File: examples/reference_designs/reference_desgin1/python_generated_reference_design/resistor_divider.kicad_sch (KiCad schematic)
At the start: 3 parts

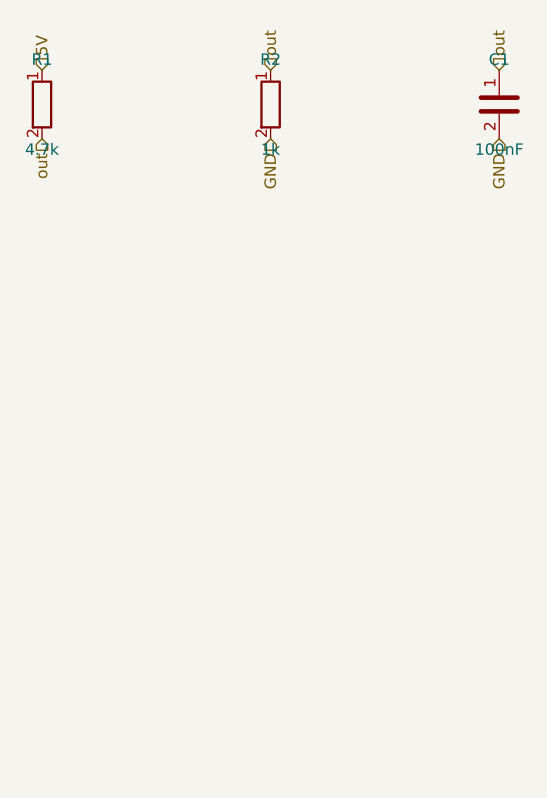
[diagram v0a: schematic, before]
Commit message: Fix component synchronization issue in reference design
Fixed issue where extra resistor components were being added back to KiCad
schematic after manual deletion. The problem was in the Python circuit
definition having both resistors with the same reference prefix "R",
causing synchronization mismatch.

Changes:
- Modified python_generated_reference_design.py to define only desired components
- Changed second resistor to explicit reference "R2" instead of prefix "R"
- Removed first resistor (r1) and its connections from circuit definition
- Updated project files to reflect synchronized state

🤖 Generated with [Claude Code](https://claude.ai/code)

Co-Authored-By: Claude <noreply@anthropic.com>
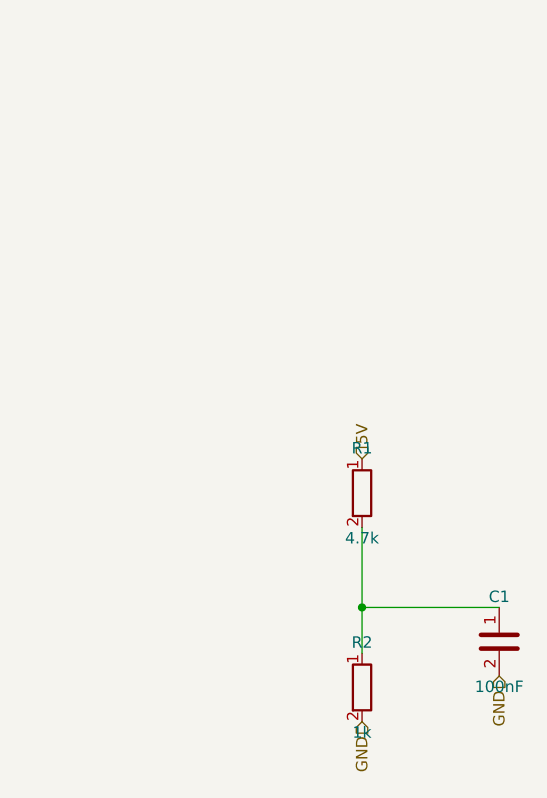
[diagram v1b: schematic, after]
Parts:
- C1, R1, R2: now left out of the parts list
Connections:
- net out: no longer names the net of C1.1, R1.2, R2.1
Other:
- company: (none) -> Circuit-Synth
- title: (none) -> resistor_divider
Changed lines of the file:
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@@
 (kicad_sch
 	(version 20250114)
-	(generator "circuit_synth")
+	(generator "eeschema")
 	(generator_version 9.0)
 	(paper A4)
+	(title_block
+		(title resistor_divider)
+		(date 2025-07-26)
+		(company Circuit-Synth)
+	)
 	(symbol
 		(lib_id Device:R)
-		(at 25.4 25.4 0)
-		(in_bom yes)
-		(on_board yes)
+		(at 60.96 90.17 0)
+		(in_bom no)
+		(on_board no)
+		(dnp no)
+		(property
+			"Reference"
+			"R2"
+			(at 60.96 85.17 0)
+			(effects
+				(font
+					(size 1.27 1.27)
+				)
+			)
+		)
+		(property
+			"Value"
+			"1k"
+			(at 60.96 95.17 0)
+			(effects
+				(font
+					(size 1.27 1.27)
+				)
+			)
+		)
+		(property
+			"Footprint"
+			"Resistor_SMD:R_0603_1608Metric"
+			(at 60.96 100.17 0)
+			(effects
+				(font
+					(size 1.27 1.27)
+				)
+				(hide yes)
+			)
+		)
+		(instances)
+	)
+	(symbol
+		(lib_id Device:C)
+		(at 76.2 85.09 0)
+		(in_bom no)
+		(on_board no)
+		(dnp no)
+		(property
+			"Reference"
+			"C1"
+			(at 76.2 80.09 0)
+			(effects
+				(font
+					(size 1.27 1.27)
+				)
+			)
+		)
+		(property
+			"Value"
+			"100nF"
+			(at 76.2 90.09 0)
+			(effects
+				(font
+					(size 1.27 1.27)
+				)
+			)
+		)
+		(property
+			"Footprint"
+			"Capacitor_SMD:C_0603_1608Metric"
+			(at 76.2 95.09 0)
+			(effects
+				(font
+					(size 1.27 1.27)
+				)
+				(hide yes)
+			)
+		)
+		(instances)
+	)
+	(symbol
+		(lib_id Device:R)
+		(at 60.96 68.58 0)
+		(in_bom no)
+		(on_board no)
 		(dnp no)
 		(property
 			"Reference"
 			"R1"
-			(at 25.4 20.4 0)
+			(at 60.96 63.58 0)
 			(effects
 				(font
@@
 			"Value"
 			"4.7k"
-			(at 25.4 30.4 0)
+			(at 60.96 73.58 0)
 			(effects
 				(font
@@
 			"Footprint"
 			"Resistor_SMD:R_0603_1608Metric"
-			(at 25.4 35.4 0)
+			(at 60.96 78.58 0)
 			(effects
 				(font
@@
 			)
 		)
-		(instances
-			(project
-				"python_generated_reference_design"
-				(path
-					"/548f32ab-3b72-47b6-b7c9-f49e04bff365/2b5db3a5-2db6-41cd-8ca2-ff5d8aed297d"
-					(reference R1)
-					(unit 1)
-				)
-			)
+		(instances)
+	)
+	(wire
+		(pts
+			(xy 60.96 81.28)
+			(xy 60.96 72.39)
+		)
+		(stroke
+			(width 0)
+			(type default)
 		)
 	)
-	(symbol
-		(lib_id Device:R)
-		(at 50.8 25.4 0)
-		(in_bom yes)
-		(on_board yes)
-		(dnp no)
-		(property
-			"Reference"
-			"R2"
-			(at 50.8 20.4 0)
-			(effects
-				(font
-					(size 1.27 1.27)
-				)
-			)
+	(wire
+		(pts
+			(xy 76.2 81.28)
+			(xy 60.96 81.28)
 		)
-		(property
-			"Value"
-			"1k"
-			(at 50.8 30.4 0)
-			(effects
-				(font
-					(size 1.27 1.27)
-				)
-			)
-		)
-		(property
-			"Footprint"
-			"Resistor_SMD:R_0603_1608Metric"
-			(at 50.8 35.4 0)
-			(effects
-				(font
-					(size 1.27 1.27)
-				)
-				(hide yes)
-			)
-		)
-		(instances
-			(project
-				"python_generated_reference_design"
-				(path
-					"/548f32ab-3b72-47b6-b7c9-f49e04bff365/2b5db3a5-2db6-41cd-8ca2-ff5d8aed297d"
-					(reference R2)
-					(unit 1)
-				)
-			)
+		(stroke
+			(width 0)
+			(type default)
 		)
 	)
-	(symbol
-		(lib_id Device:C)
-		(at 76.2 25.4 0)
-		(in_bom yes)
-		(on_board yes)
-		(dnp no)
-		(property
-			"Reference"
-			"C1"
-			(at 76.2 20.4 0)
-			(effects
-				(font
-					(size 1.27 1.27)
-				)
-			)
+	(wire
+		(pts
+			(xy 60.96 81.28)
+			(xy 60.96 86.36)
 		)
-		(property
-			"Value"
-			"100nF"
-			(at 76.2 30.4 0)
-			(effects
-				(font
-					(size 1.27 1.27)
-				)
-			)
-		)
-		(property
-			"Footprint"
-			"Capacitor_SMD:C_0603_1608Metric"
-			(at 76.2 35.4 0)
-			(effects
-				(font
-					(size 1.27 1.27)
-				)
-				(hide yes)
-			)
-		)
-		(instances
-			(project
-				"python_generated_reference_design"
-				(path
-					"/548f32ab-3b72-47b6-b7c9-f49e04bff365/2b5db3a5-2db6-41cd-8ca2-ff5d8aed297d"
-					(reference C1)
-					(unit 1)
-				)
-			)
+		(stroke
+			(width 0)
+			(type default)
 		)
 	)
@@
 		5V
 		(shape input)
-		(at 25.4 21.59 90)
-		(effects
-			(font
-				(size 1.27 1.27)
-			)
-			(justify left)
-		)
-	)
-	(hierarchical_label
-		out
-		(shape input)
-		(at 76.2 21.59 90)
-		(effects
-			(font
-				(size 1.27 1.27)
-			)
-			(justify left)
-		)
-	)
-	(hierarchical_label
-		out
-		(shape input)
-		(at 25.4 29.209999999999997 270)
-		(effects
-			(font
-				(size 1.27 1.27)
-			)
-			(justify right)
-		)
-	)
-	(hierarchical_label
-		out
-		(shape input)
-		(at 50.8 21.59 90)
+		(at 60.96 64.77 90)
 		(effects
 			(font
@@
 		GND
 		(shape input)
-		(at 76.2 29.209999999999997 270)
+		(at 60.96 93.98 270)
 		(effects
 			(font
@@
 		GND
 		(shape input)
-		(at 50.8 29.209999999999997 270)
+		(at 76.2 88.9 270)
 		(effects
 			(font
@@
 		)
 	)
+	(junction
+		(at 60.96 81.28)
+		(diameter 0)
+	)
 	(sheet_instances

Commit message: Update KiCad schematic with corrected component flags and instance data
- Updated resistor_divider.kicad_sch with proper in_bom=yes and on_board=yes flags
- Added proper instance information with correct project hierarchy paths
- Enhanced s_expression parser with detailed instance processing logging
- Components now display correctly as R1, R2, C1 instead of "?" symbols

This completes the component reference display fix ensuring professional
schematic appearance in KiCad.

🤖 Generated with [Claude Code](https://claude.ai/code)

Co-Authored-By: Claude <noreply@anthropic.com>
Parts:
- C1, R1, R2: now in the parts list
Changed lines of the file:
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@@
 		(lib_id Device:R)
 		(at 60.96 90.17 0)
-		(in_bom no)
-		(on_board no)
+		(in_bom yes)
+		(on_board yes)
 		(dnp no)
 		(property
@@
 			)
 		)
-		(instances)
+		(instances
+			(project
+				"090c2e97-1b39-4ce2-a8e2-7c82eb1d5b33"
+				(path
+					"/090c2e97-1b39-4ce2-a8e2-7c82eb1d5b33/9dc51fe2-5b74-4dc5-925d-ec0371140177"
+					(reference R2)
+					(unit 1)
+				)
+			)
+		)
 	)
 	(symbol
 		(lib_id Device:C)
 		(at 76.2 85.09 0)
-		(in_bom no)
-		(on_board no)
+		(in_bom yes)
+		(on_board yes)
 		(dnp no)
 		(property
@@
 			)
 		)
-		(instances)
+		(instances
+			(project
+				"090c2e97-1b39-4ce2-a8e2-7c82eb1d5b33"
+				(path
+					"/090c2e97-1b39-4ce2-a8e2-7c82eb1d5b33/9dc51fe2-5b74-4dc5-925d-ec0371140177"
+					(reference C1)
+					(unit 1)
+				)
+			)
+		)
 	)
 	(symbol
 		(lib_id Device:R)
 		(at 60.96 68.58 0)
-		(in_bom no)
-		(on_board no)
+		(in_bom yes)
+		(on_board yes)
 		(dnp no)
 		(property
@@
 			)
 		)
-		(instances)
+		(instances
+			(project
+				"090c2e97-1b39-4ce2-a8e2-7c82eb1d5b33"
+				(path
+					"/090c2e97-1b39-4ce2-a8e2-7c82eb1d5b33/9dc51fe2-5b74-4dc5-925d-ec0371140177"
+					(reference R1)
+					(unit 1)
+				)
+			)
+		)
 	)
 	(wire
